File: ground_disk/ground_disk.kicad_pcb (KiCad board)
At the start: 2 copper layers, 150 x 150 mm, 0 parts

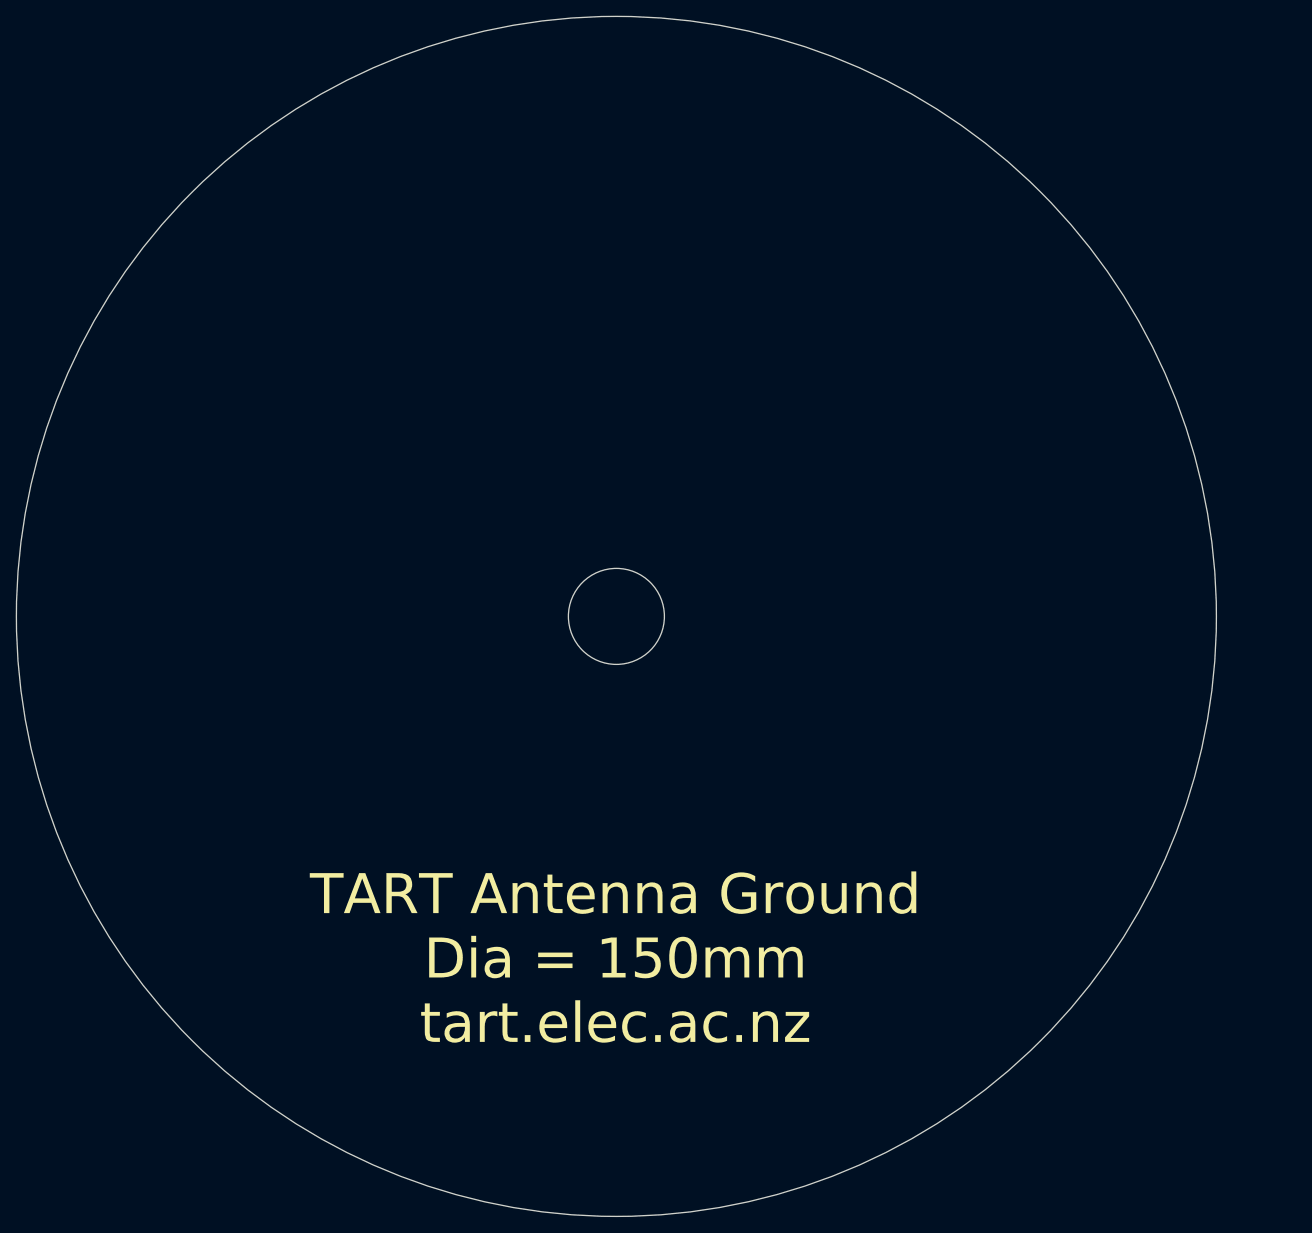
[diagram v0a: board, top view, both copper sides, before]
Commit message: Add grid of holes for drainage
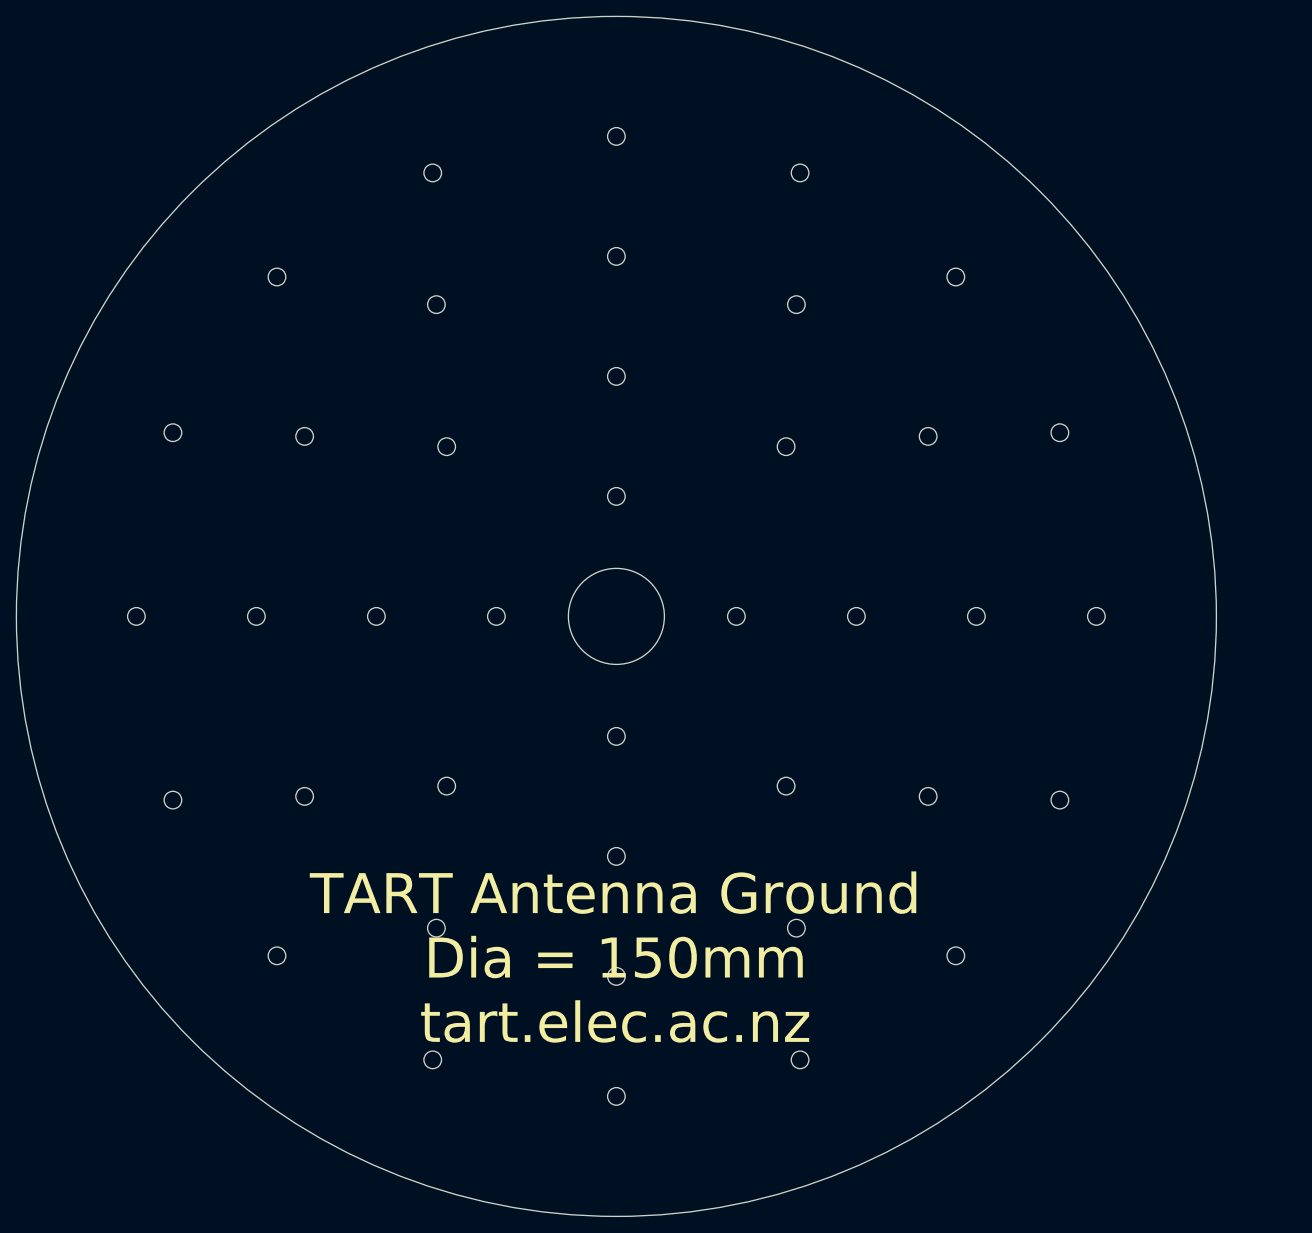
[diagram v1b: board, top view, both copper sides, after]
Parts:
- added REF**: , MountingHole:MountingHole_2.2mm_M2, F.Cu at (170.0, 100.0)
- added REF**: , MountingHole:MountingHole_2.2mm_M2, F.Cu at (140.0, 100.0)
- added REF**: , MountingHole:MountingHole_2.2mm_M2, F.Cu at (155.0, 100.0)
- added REF**: , MountingHole:MountingHole_2.2mm_M2, F.Cu at (185.0, 100.0)
- added REF**1: , MountingHole:MountingHole_2.2mm_M2, F.Cu at (125.0, 85.0)
- added REF**10: , MountingHole:MountingHole_2.2mm_M2, F.Cu at (146.2, 121.2)
- added REF**11: , MountingHole:MountingHole_2.2mm_M2, F.Cu at (164.0, 77.5)
- added REF**12: , MountingHole:MountingHole_2.2mm_M2, F.Cu at (147.5, 61.0)
- added REF**13: , MountingHole:MountingHole_2.2mm_M2, F.Cu at (125.0, 55.0)
- added REF**14: , MountingHole:MountingHole_2.2mm_M2, F.Cu at (102.5, 61.0)
- added REF**15: , MountingHole:MountingHole_2.2mm_M2, F.Cu at (86.0, 77.5)
- added REF**16: , MountingHole:MountingHole_2.2mm_M2, F.Cu at (80.0, 100.0)
- added REF**17: , MountingHole:MountingHole_2.2mm_M2, F.Cu at (86.0, 122.5)
- added REF**18: , MountingHole:MountingHole_2.2mm_M2, F.Cu at (102.5, 139.0)
- added REF**19: , MountingHole:MountingHole_2.2mm_M2, F.Cu at (125.0, 145.0)
- added REF**2: , MountingHole:MountingHole_2.2mm_M2, F.Cu at (110.0, 100.0)
- added REF**20: , MountingHole:MountingHole_2.2mm_M2, F.Cu at (147.5, 139.0)
- added REF**21: , MountingHole:MountingHole_2.2mm_M2, F.Cu at (164.0, 122.5)
- added REF**22: , MountingHole:MountingHole_2.2mm_M2, F.Cu at (180.4, 77.0)
- added REF**23: , MountingHole:MountingHole_2.2mm_M2, F.Cu at (167.4, 57.6)
- added REF**24: , MountingHole:MountingHole_2.2mm_M2, F.Cu at (148.0, 44.6)
- added REF**25: , MountingHole:MountingHole_2.2mm_M2, F.Cu at (125.0, 40.0)
- added REF**26: , MountingHole:MountingHole_2.2mm_M2, F.Cu at (102.0, 44.6)
- added REF**27: , MountingHole:MountingHole_2.2mm_M2, F.Cu at (82.6, 57.6)
- added REF**28: , MountingHole:MountingHole_2.2mm_M2, F.Cu at (69.6, 77.0)
- added REF**29: , MountingHole:MountingHole_2.2mm_M2, F.Cu at (65.0, 100.0)
- added REF**3: , MountingHole:MountingHole_2.2mm_M2, F.Cu at (125.0, 115.0)
- added REF**30: , MountingHole:MountingHole_2.2mm_M2, F.Cu at (69.6, 123.0)
- added REF**31: , MountingHole:MountingHole_2.2mm_M2, F.Cu at (82.6, 142.4)
- added REF**32: , MountingHole:MountingHole_2.2mm_M2, F.Cu at (102.0, 155.4)
- added REF**33: , MountingHole:MountingHole_2.2mm_M2, F.Cu at (125.0, 160.0)
- added REF**34: , MountingHole:MountingHole_2.2mm_M2, F.Cu at (148.0, 155.4)
- added REF**35: , MountingHole:MountingHole_2.2mm_M2, F.Cu at (167.4, 142.4)
- added REF**36: , MountingHole:MountingHole_2.2mm_M2, F.Cu at (180.4, 123.0)
- added REF**4: , MountingHole:MountingHole_2.2mm_M2, F.Cu at (146.2, 78.8)
- added REF**5: , MountingHole:MountingHole_2.2mm_M2, F.Cu at (125.0, 70.0)
- added REF**6: , MountingHole:MountingHole_2.2mm_M2, F.Cu at (103.8, 78.8)
- added REF**7: , MountingHole:MountingHole_2.2mm_M2, F.Cu at (95.0, 100.0)
- added REF**8: , MountingHole:MountingHole_2.2mm_M2, F.Cu at (103.8, 121.2)
- added REF**9: , MountingHole:MountingHole_2.2mm_M2, F.Cu at (125.0, 130.0)

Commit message: Reduced dimensions, and increased hole size to lighten disk
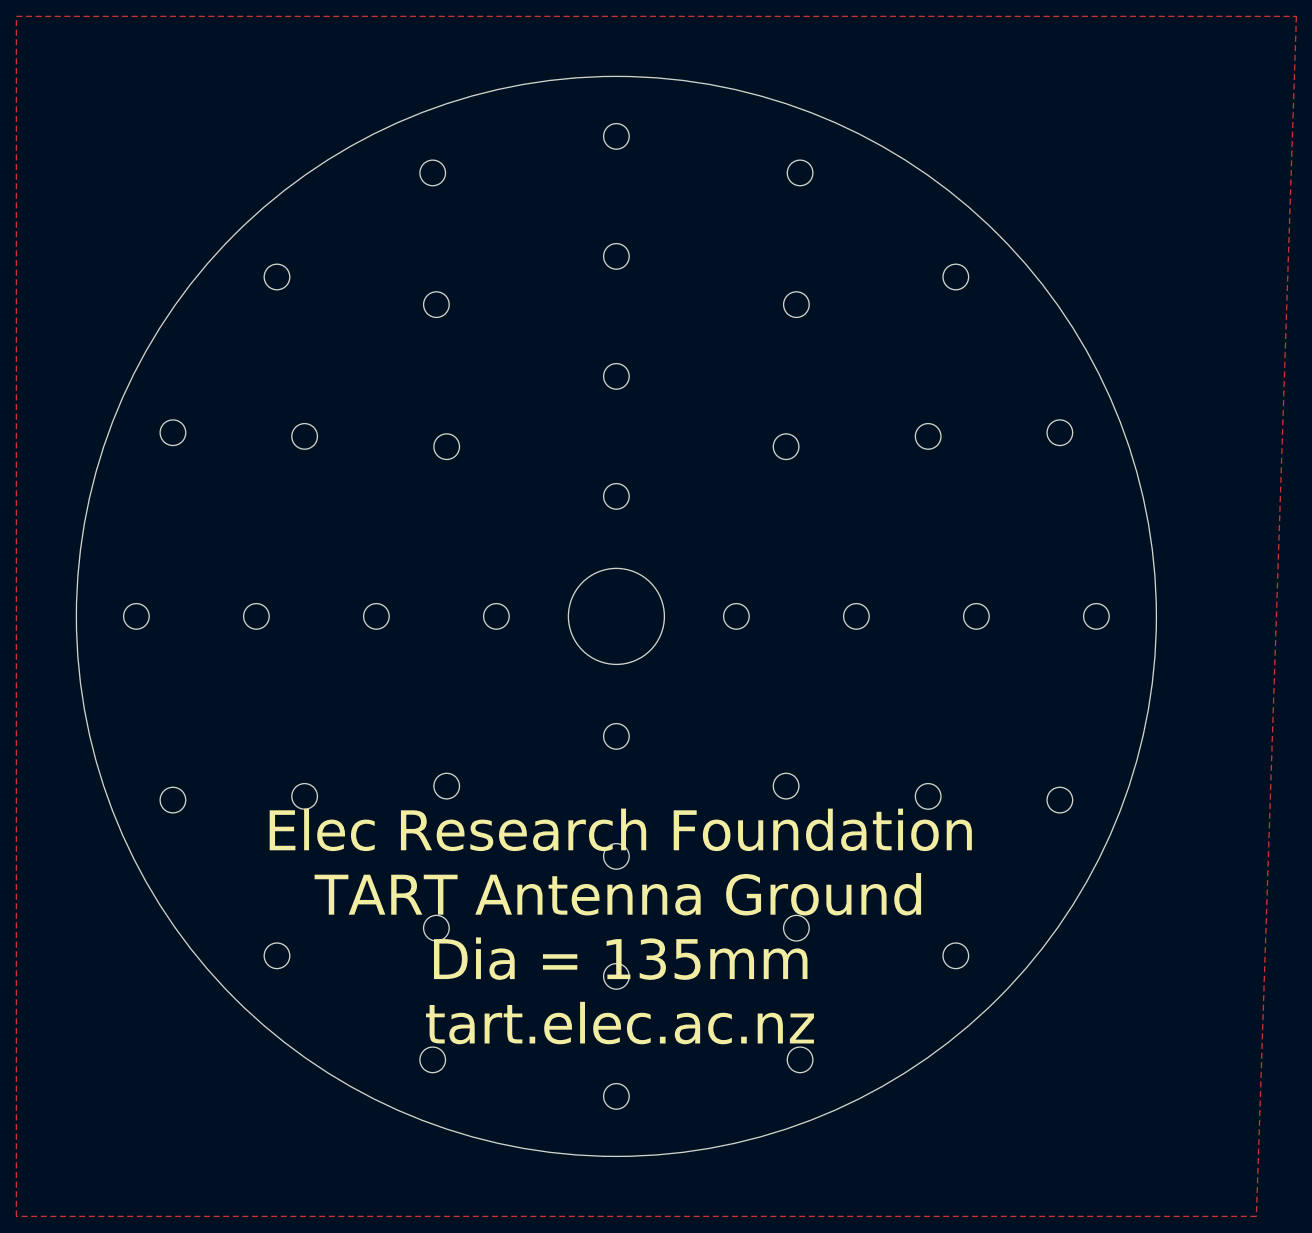
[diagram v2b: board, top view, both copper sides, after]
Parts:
- REF** (x4), REF**1, REF**10, REF**11, REF**12, REF**13, REF**14, REF**15, REF**16, REF**17, REF**18, REF**19, REF**2, REF**20, REF**21, REF**22, REF**23, REF**24, REF**25, REF**26, REF**27, REF**28, REF**29, REF**3, REF**30, REF**31, REF**32, REF**33, REF**34, REF**35, REF**36, REF**4, REF**5, REF**6, REF**7, REF**8, REF**9: footprint MountingHole:MountingHole_2.2mm_M2 -> MountingHole:MountingHole_3.2mm_M3
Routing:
- added copper zone on F.Cu, net (none)
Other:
- board size 150 x 150 mm -> 135 x 135 mm
- board text added: "Elec Research Foundation TART Antenna Ground Dia = 135mm tart.elec.ac.nz"
- board text removed: "TART Antenna Ground Dia = 150mm tart.elec.ac.nz"
